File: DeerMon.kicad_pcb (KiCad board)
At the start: 4 copper layers, 30 x 30 mm, 47 parts, among them J1 TYPE-C-31-M-12, J2 ZJY144S025, J3 GPIO, Q1 BC847BVC-7, Q2 2N7002, SW1 BOOT, SW2 EN, U1 CP2102N-A02-GQFN24R, U2 AW9364DNR, U3 SPX3819M5-L-3-3, U4 ESP32-PICO-V3-02

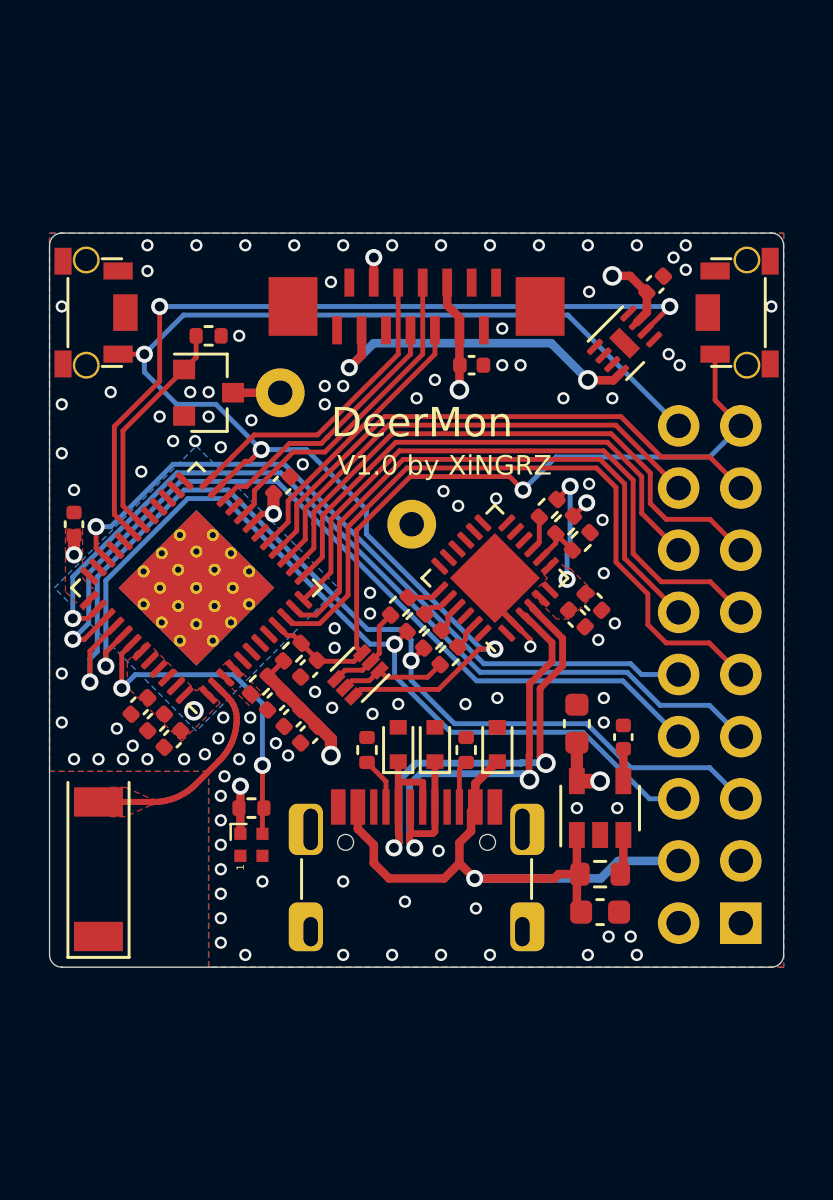
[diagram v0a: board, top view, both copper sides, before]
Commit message: Adjust outline for buttons
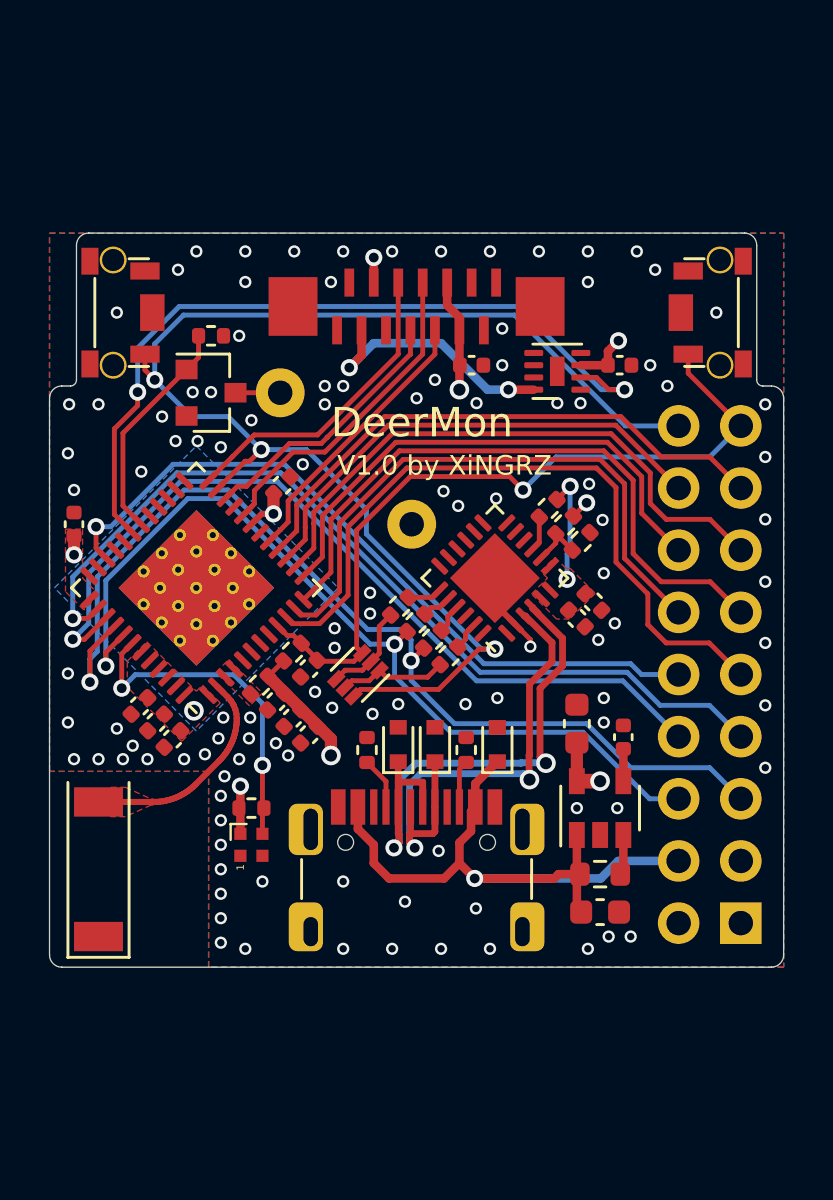
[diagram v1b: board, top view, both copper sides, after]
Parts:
- moved C8 3.60 mm to (73.3, 55.4), turned to 0 degrees
- moved U2 2.98 mm to (70.8, 55.6), turned to 180 degrees
- moved SW1 1.10 mm to (52.6, 53.2)
- moved SW2 1.10 mm to (77.4, 53.2)
- moved Q2 0.10 mm to (56.6, 56.5)
- moved R13 0.10 mm to (56.6, 54.2)
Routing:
- net +3V3: track 118.8 -> 113.1 mm
- net /LEDK: track 14.0 -> 10.5 mm
- net GND: vias 108 -> 111
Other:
- outline, holes or cut-outs redrawn

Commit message: Add M1 mount points
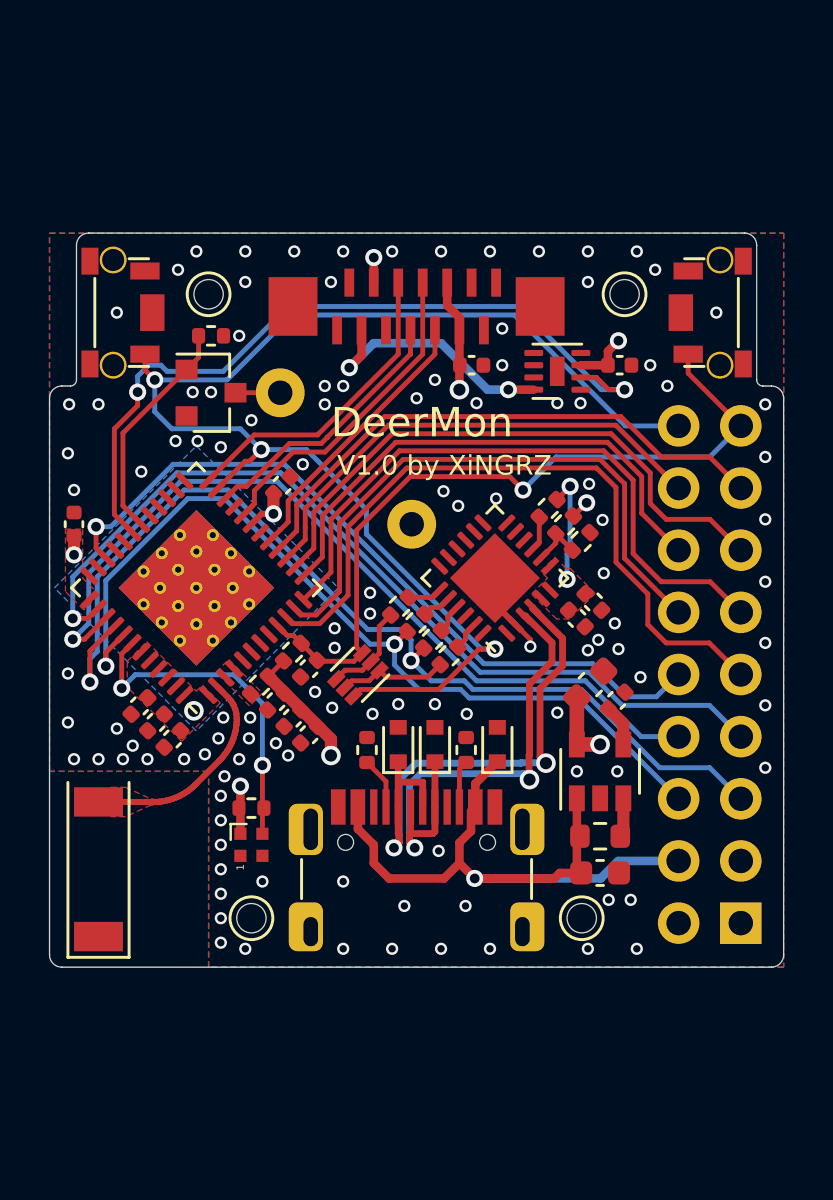
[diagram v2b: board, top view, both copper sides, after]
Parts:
- moved C10 1.69 mm to (72.1, 68.5), turned to 45 degrees
- moved C9 1.60 mm to (72.5, 76.2)
- moved R14 1.55 mm to (72.5, 74.7)
- moved C4 1.53 mm to (73.2, 69.1), turned to 45 degrees
- moved U3 1.50 mm to (72.5, 72.0)
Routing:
- net +3V3: track 113.1 -> 114.3 mm
- net /IO5: track 30.4 -> 31.2 mm
- net +5V: track 52.4 -> 53.1 mm
- net GND: vias 111 -> 113
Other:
- outline, holes or cut-outs redrawn
- board text added: "5V 3V3"
- board text added: "BOOT 26 33 35 5 22 TX"
- board text removed: "BOOT 26 33 35 5 22 TX 5V 3V3"

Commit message: Add craft edges and JLCJLCJLCJLC
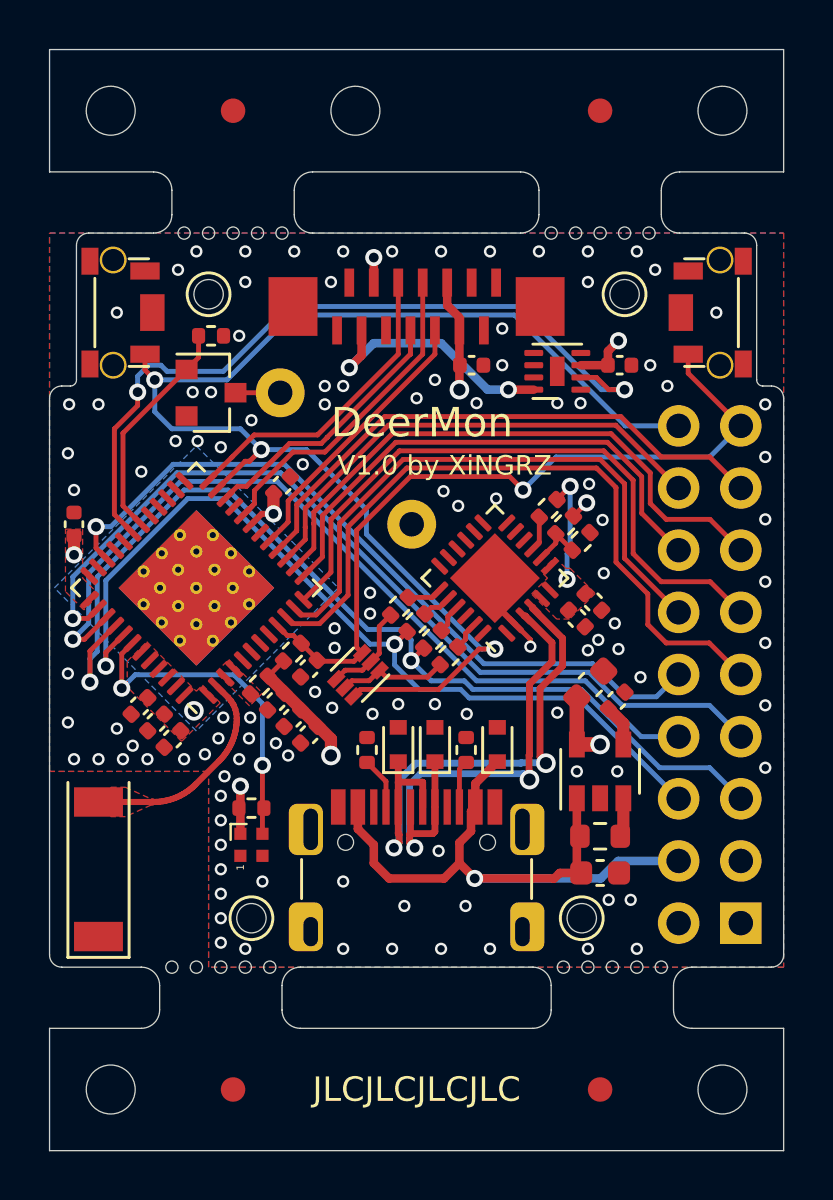
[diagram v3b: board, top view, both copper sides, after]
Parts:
- added H1: Mark, JLC-SMT:MARK, F.Cu at (57.5, 45.0)
- added H2: Mark, JLC-SMT:MARK, F.Cu at (57.5, 85.0)
- added H3: Mark, JLC-SMT:MARK, F.Cu at (72.5, 45.0)
- added H4: Mark, JLC-SMT:MARK, F.Cu at (72.5, 85.0)
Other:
- board size 30 x 30 mm -> 30 x 45 mm
- board text added: "JLCJLCJLCJLC"

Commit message: Use mechanical drills instead of outline for mounting and positioning
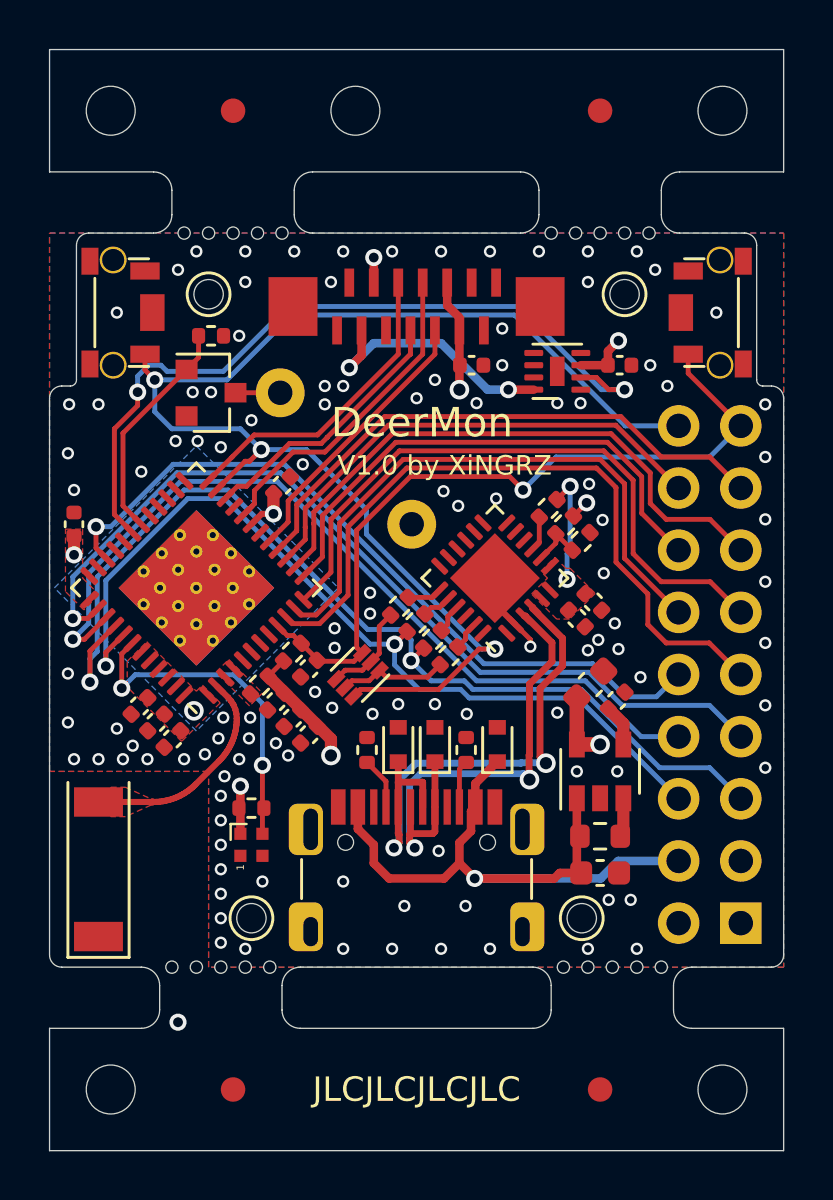
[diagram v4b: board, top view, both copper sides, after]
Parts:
- added CE1: CraftEdge, JLC-SMT:JLC_CRAFT_EDGE, F.Cu at (57.5, 50.0)
- added CE2: CraftEdge, JLC-SMT:JLC_CRAFT_EDGE, F.Cu at (57.0, 80.0)
- added CE3: CraftEdge, JLC-SMT:JLC_CRAFT_EDGE, F.Cu at (72.5, 50.0)
- added CE4: CraftEdge, JLC-SMT:JLC_CRAFT_EDGE, F.Cu at (73.0, 80.0)
- added H2: Mount, JLC-SMT:MountingHole_1.2mm_M1, F.Cu at (73.5, 52.5)
- added H3: Mount, JLC-SMT:MountingHole_1.2mm_M1, F.Cu at (58.2, 78.0)
- added H4: Mount, JLC-SMT:MountingHole_1.2mm_M1, F.Cu at (71.8, 78.0)
- added M1: Mark, JLC-SMT:JLC_MARK, F.Cu at (57.5, 45.0)
- added P1: Position, JLC-SMT:JLC_POS, F.Cu at (77.5, 85.0)
- added P2: Position, JLC-SMT:JLC_POS, F.Cu at (52.5, 85.0)
- added P3: Position, JLC-SMT:JLC_POS, F.Cu at (77.5, 45.0)
- added P4: Position, JLC-SMT:JLC_POS, F.Cu at (52.5, 45.0)
- added P5: Position, JLC-SMT:JLC_POS, F.Cu at (62.5, 45.0)
- H1: value Mark -> Mount; footprint JLC-SMT:MARK -> JLC-SMT:MountingHole_1.2mm_M1
- M2: renamed from H2; footprint JLC-SMT:MARK -> JLC-SMT:JLC_MARK
- M3: renamed from H3; footprint JLC-SMT:MARK -> JLC-SMT:JLC_MARK
- M4: renamed from H4; footprint JLC-SMT:MARK -> JLC-SMT:JLC_MARK
- moved H1 7.57 mm to (56.5, 52.5)
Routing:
- net (no net): vias 0 -> 1
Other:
- outline, holes or cut-outs redrawn

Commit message: Use IO19/22 instead of reserved IO6/11 for BLK and BZ_EN
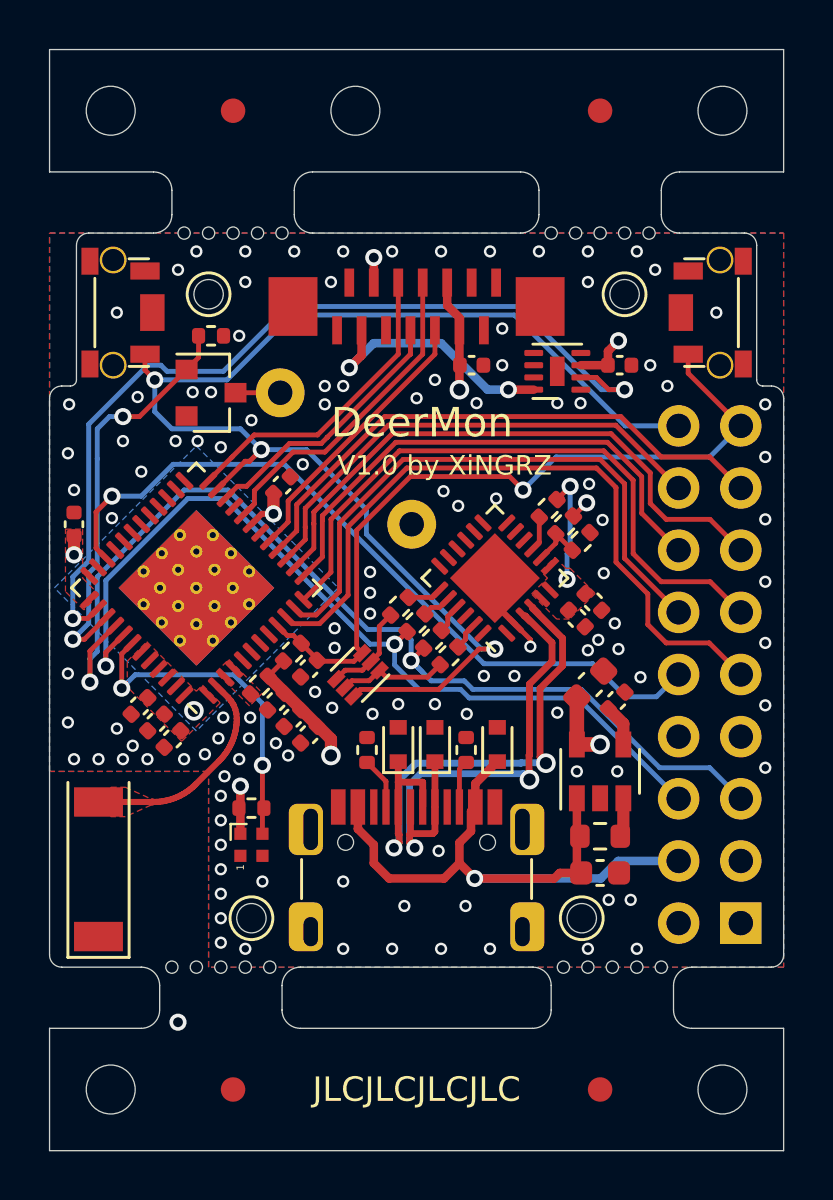
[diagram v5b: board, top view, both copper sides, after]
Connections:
- J3 pad 7: /IO19 -> GND
- J3 pad 8: /IO22 -> GND
- U4 pad 30: /BZ_EN -> (no net)
- U4 pad 31: /BLK -> (no net)
- U4 pad 38: /IO19 -> /BLK
- U4 pad 39: /IO22 -> /BZ_EN
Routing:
- net /IO19: track 36.4 -> 0.00 mm, vias 1 -> 0
- net /IO22: track 34.7 -> 0.00 mm, vias 1 -> 0
- net /BZ_EN: track 9.28 -> 17.0 mm, vias 0 -> 2
- net /BLK: track 31.8 -> 36.9 mm
- net /ESP_RX: track 41.4 -> 42.1 mm
- net GND: vias 113 -> 118

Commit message: Use DDC114TH instead of BC847BVC, with position of 10K resistor fixed
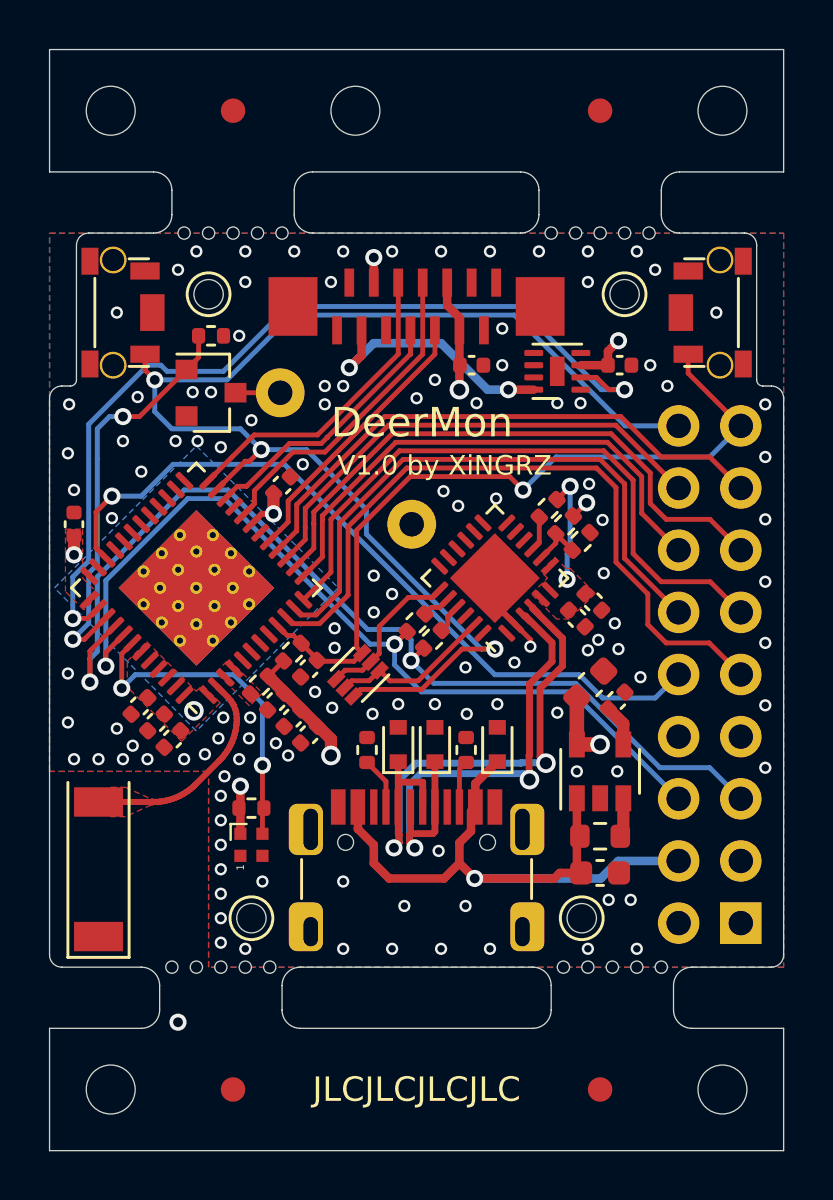
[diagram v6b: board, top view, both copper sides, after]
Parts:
- removed R6, R9: 10K, Resistor_SMD:R_0402_1005Metric
- Q1: value BC847BVC-7 -> DDC114TH
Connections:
- Q1 pad 1: Net-(Q1-Pad1) -> /DTR
- Q1 pad 2: Net-(Q1-Pad2) -> /RTS
- Q1 pad 4: Net-(Q1-Pad2) -> /RTS
- Q1 pad 5: Net-(Q1-Pad1) -> /DTR
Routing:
- net /DTR: track 1.19 -> 6.71 mm
- net /RTS: track 1.41 -> 6.38 mm
- net Net-(Q1-Pad1): track 4.52 -> 0.00 mm
- net Net-(Q1-Pad2): track 3.95 -> 0.00 mm
- net /ESP_RX: track 42.1 -> 41.4 mm
- net GND: vias 118 -> 119

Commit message: Better tracks
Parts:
- moved Q1 3.83 mm to (66.4, 67.6), turned to 315 degrees
- moved R7 0.66 mm to (64.4, 65.6)
- moved R8 0.63 mm to (65.1, 66.3)
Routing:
- net /BOOT: track 54.6 -> 48.2 mm
- net /RTS: track 6.38 -> 12.0 mm, vias 0 -> 2
- net /EN: track 31.1 -> 35.2 mm
- net /DTR: track 6.71 -> 3.14 mm
- net GND: vias 119 -> 116
